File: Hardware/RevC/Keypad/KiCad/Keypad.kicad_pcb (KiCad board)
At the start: 2 copper layers, 100 x 100 mm, 258 parts, among them U1 PIN_STRIP_8, U2 PIN_STRIP_8, U3 PIN_STRIP_8, U31 PIN_STRIP_1, U32 PIN_STRIP_1, U33 PIN_STRIP_1, U34 PIN_STRIP_1, U35 PIN_STRIP_1, U36 PIN_STRIP_1, U37 PIN_STRIP_1, U38 PIN_STRIP_1, U4 PIN_STRIP_8, U41 PIN_STRIP_1, U42 PIN_STRIP_1, U43 PIN_STRIP_1, U44 PIN_STRIP_1, U45 PIN_STRIP_1, U46 PIN_STRIP_1, U47 PIN_STRIP_1, U48 PIN_STRIP_1

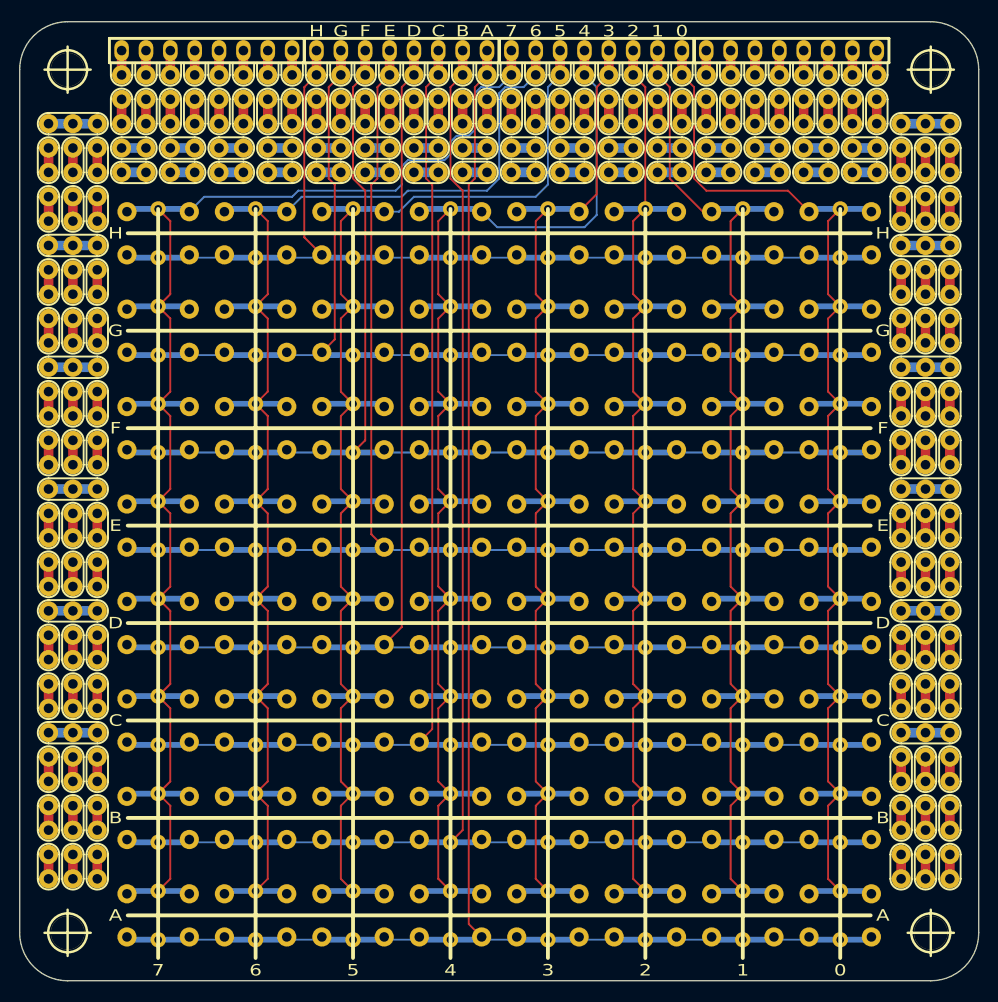
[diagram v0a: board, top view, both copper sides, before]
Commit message: added Gerber files
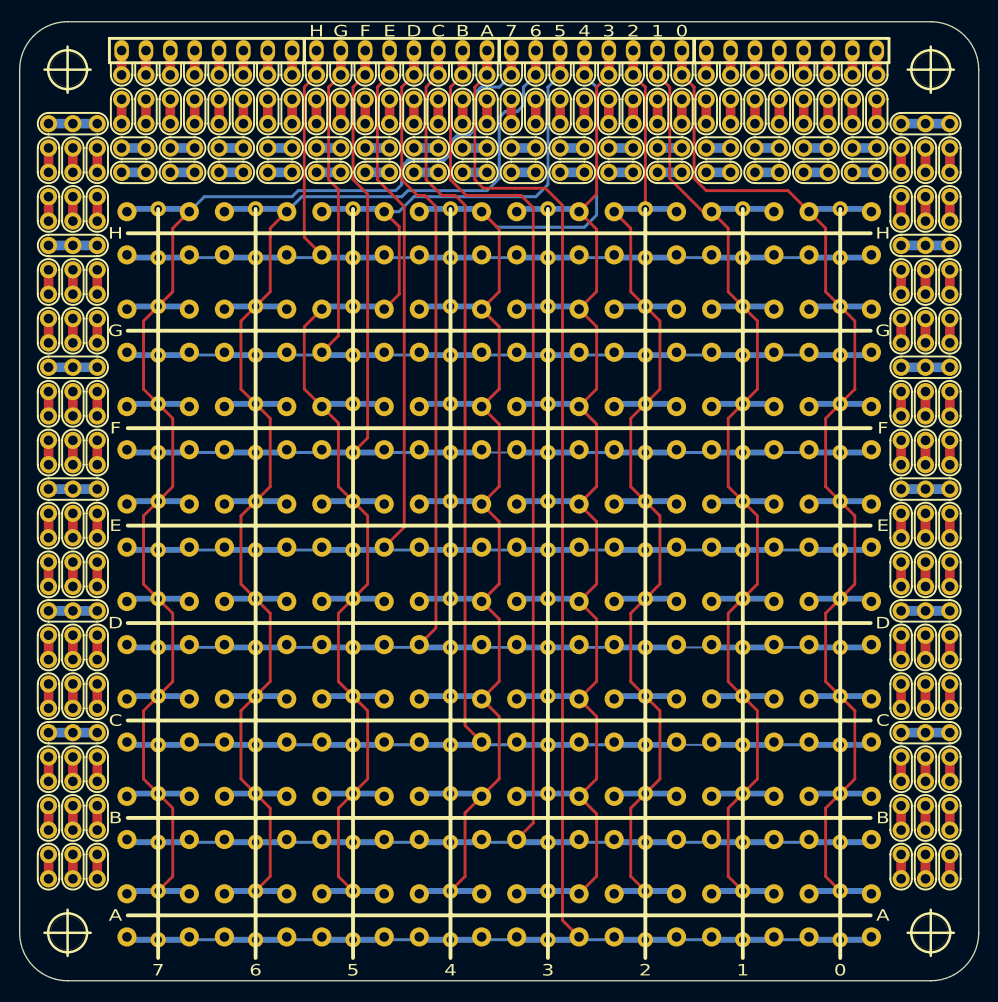
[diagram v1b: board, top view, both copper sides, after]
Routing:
- net /KEYPAD_ROW_A: track 216.3 -> 223.7 mm
- net /KEYPAD_ROW_B: track 206.6 -> 212.9 mm
- net /KEYPAD_COL_3: track 148.0 -> 151.2 mm
- net /KEYPAD_COL_4: track 160.7 -> 163.5 mm
- net /KEYPAD_ROW_C: track 195.9 -> 198.3 mm
- net /KEYPAD_ROW_D: track 185.7 -> 187.6 mm
- net /KEYPAD_COL_5: track 162.6 -> 164.2 mm
- net /KEYPAD_COL_7: track 176.0 -> 177.3 mm
- net /KEYPAD_COL_2: track 146.9 -> 148.2 mm
- net /KEYPAD_COL_1: track 149.5 -> 150.8 mm
- net /KEYPAD_COL_0: track 157.2 -> 158.4 mm
- net /KEYPAD_ROW_E: track 175.6 -> 176.8 mm
- net /KEYPAD_COL_6: track 169.5 -> 170.4 mm
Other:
- net class Default: clearance 0.16 -> 0.2; trace_width 0.2 -> 0.25
- rule trace_clearance: 0.16 -> 0.2
- rule trace_min: 0.1523 -> 0.25

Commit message: fixed keypad PCBs
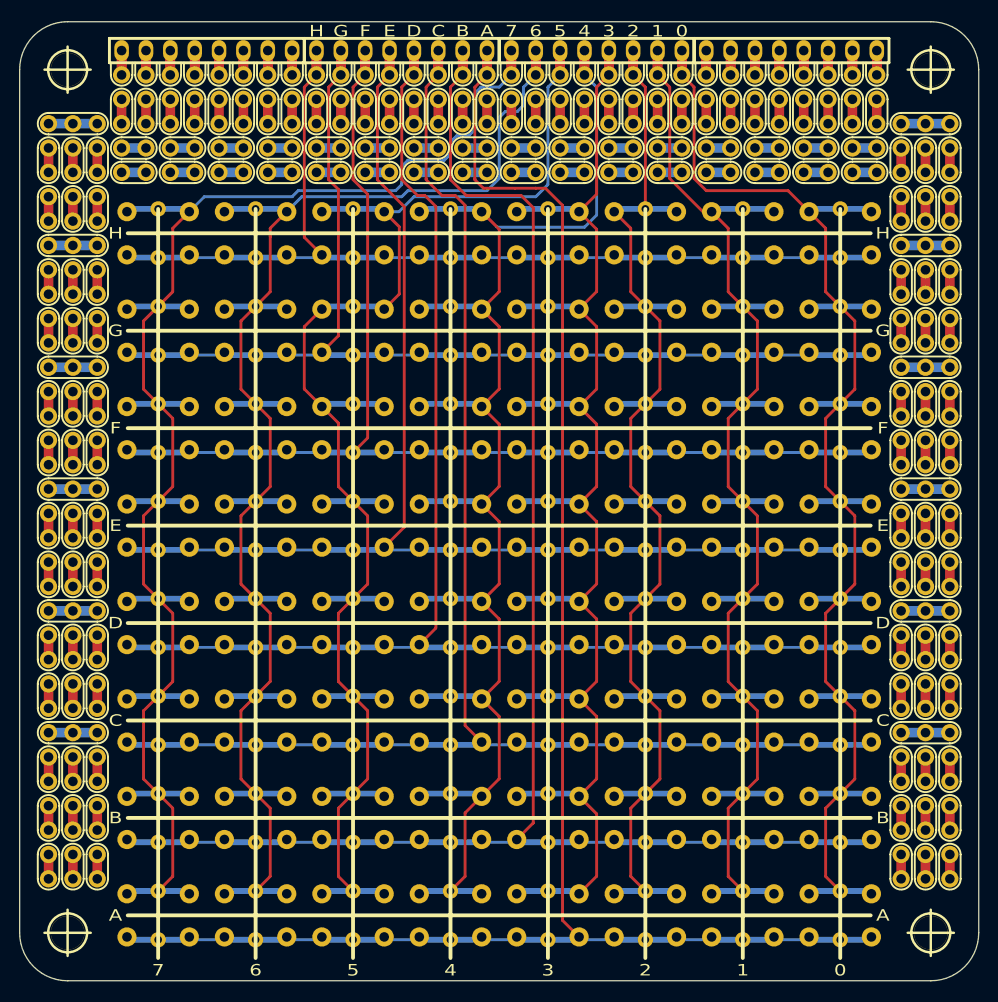
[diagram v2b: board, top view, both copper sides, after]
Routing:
- net /KEYPAD_ROW_B: track 212.9 -> 215.5 mm
- net Net-(U4-Pad8): track 0.00 -> 2.54 mm
- net Net-(U4-Pad7): track 0.00 -> 2.54 mm
- net Net-(U4-Pad6): track 0.00 -> 2.54 mm
- net Net-(U4-Pad5): track 0.00 -> 2.54 mm
- net Net-(U4-Pad4): track 0.00 -> 2.54 mm
- net Net-(U4-Pad3): track 0.00 -> 2.54 mm
- net Net-(U4-Pad2): track 0.00 -> 2.54 mm
- net Net-(U4-Pad1): track 0.00 -> 2.54 mm
- net Net-(U3-Pad8): track 0.00 -> 2.54 mm
- net Net-(U3-Pad7): track 0.00 -> 2.54 mm
- net Net-(U3-Pad6): track 0.00 -> 2.54 mm
- net Net-(U3-Pad5): track 0.00 -> 2.54 mm
- net Net-(U3-Pad4): track 0.00 -> 2.54 mm
- net Net-(U3-Pad3): track 0.00 -> 2.54 mm
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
